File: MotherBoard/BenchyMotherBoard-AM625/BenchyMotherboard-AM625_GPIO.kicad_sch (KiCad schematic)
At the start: 58 parts, among them J14 S3B-XH-A, J17 B10B-XH-A, J2 S4B-XA-SK, U1 AM6254ATCGGAALW, U38 EMC2301-1-ACZL-TR, U58 NCV7357MW3R2G, U65 74LVC541ABQ,115

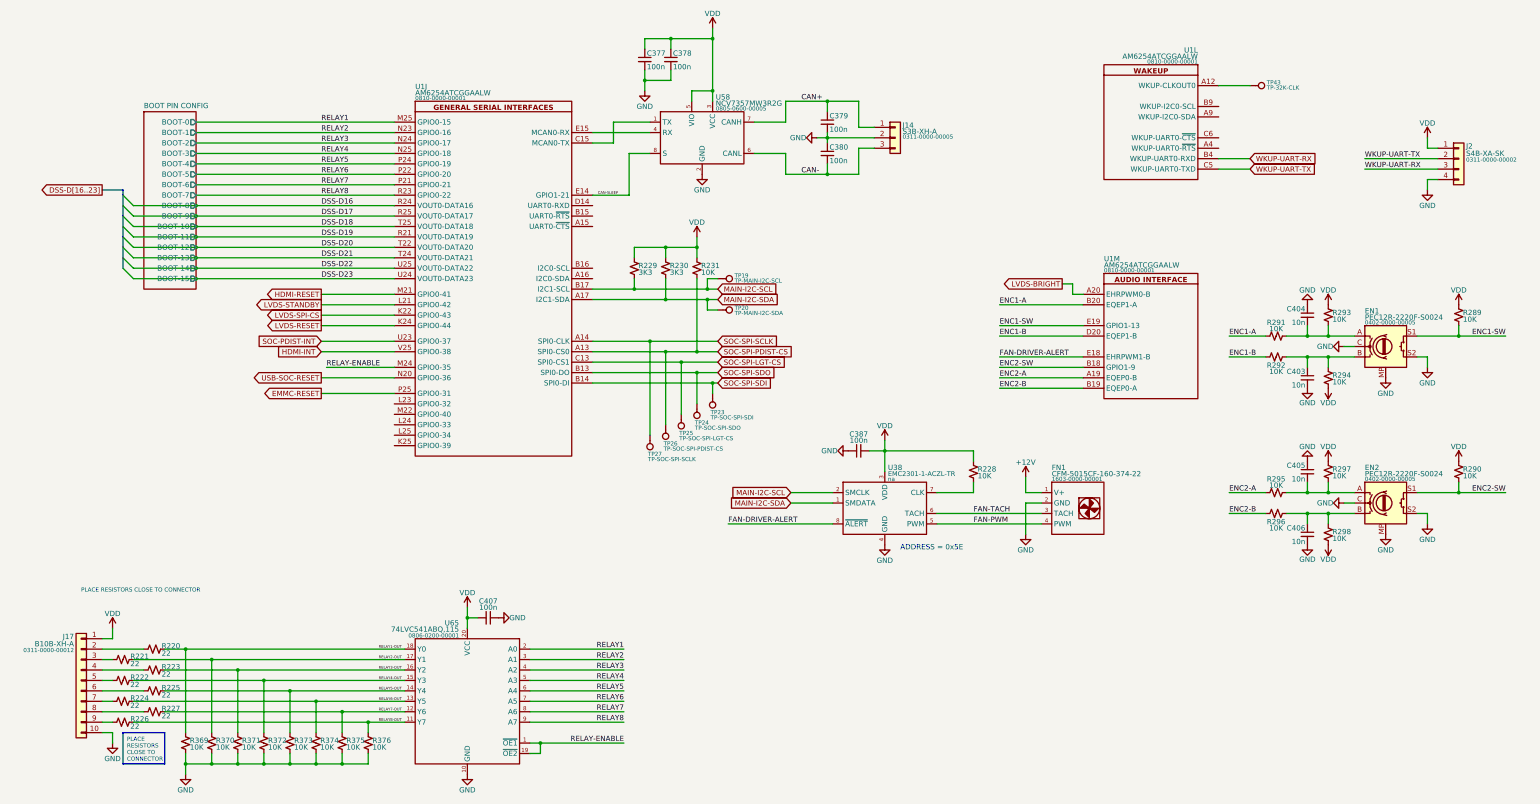
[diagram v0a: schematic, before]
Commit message: Schematic capture mostly complete. Starting PCB layout
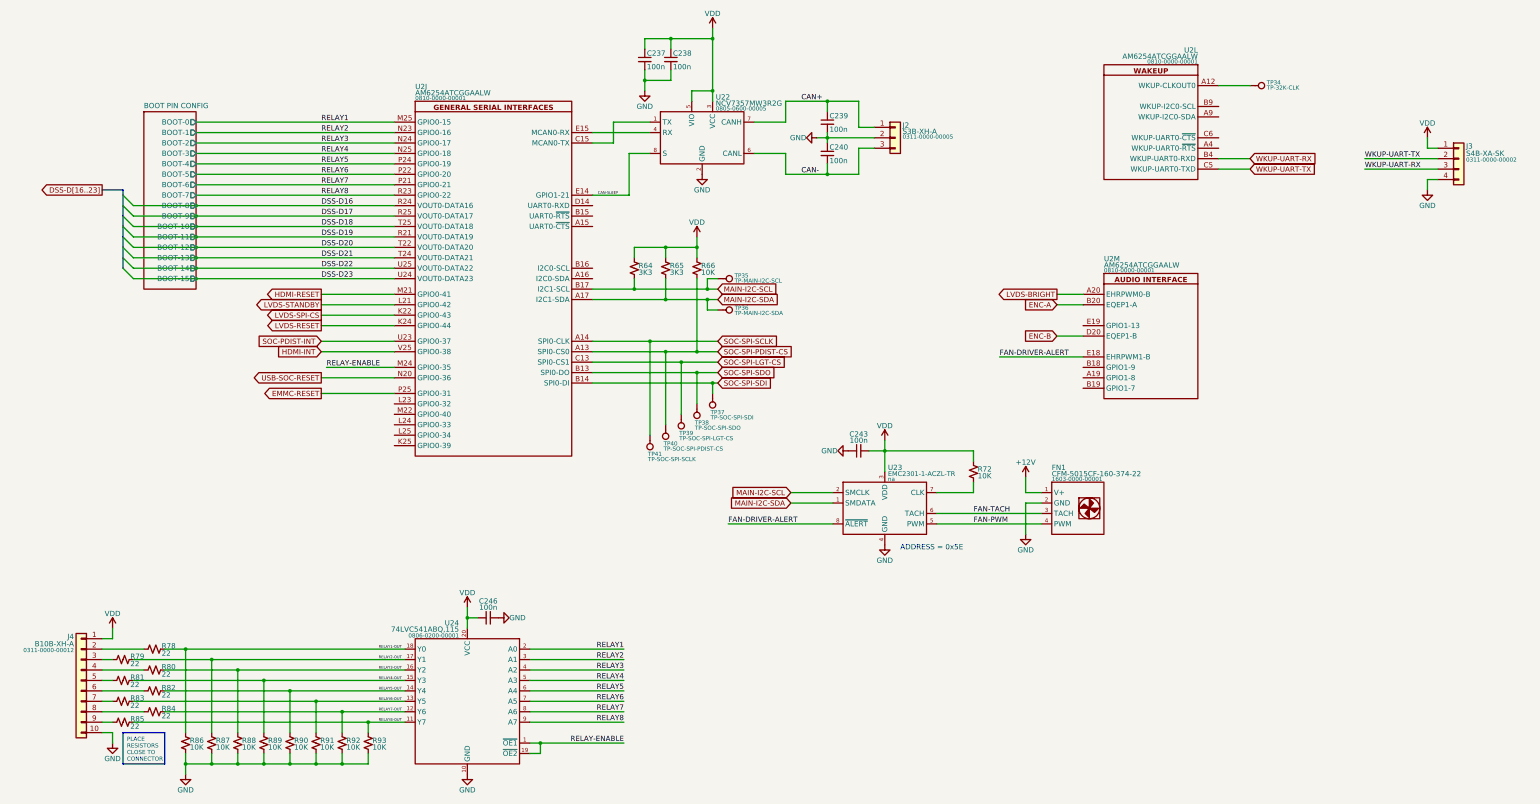
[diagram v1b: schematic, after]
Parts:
- removed C403, C404, C405, C406: 10n, Daxxn_Standard_Capacitors:CAP_0402, symbol DX_Capacitor_Ceramic:CL05B103KB5NNNC
- removed EN1, EN2: PEC12R-2220F-S0024, Daxxn_Controls_Encoders:PEC12R, symbol DX_Control_RotaryEncoder:PEC12R-2220F-S0024
- removed R289, R290, R291, R292, R293, R294, R295, R296, R297, R298: 10K, Daxxn_Standard_Resistors:RES_0402, symbol DX_Resistor:RC0402JR-0710KL
- FN1: footprint Daxxn_Connectors_JST:B4B-XH-A -> Daxxn_Connectors_Header:0470533000
- renumbered C377 to C237, C378 to C238, C379 to C239, C380 to C240, C387 to C243, C407 to C246, J14 to J2, J2 to J3, J17 to J4, R229 to R64, R230 to R65, R231 to R66, R228 to R72, R220 to R78, R221 to R79, R223 to R80, R222 to R81, R225 to R82, R224 to R83, R227 to R84, R226 to R85, R369 to R86, R370 to R87, R371 to R88, R372 to R89, R373 to R90, R374 to R91, R375 to R92, R376 to R93, TP43 to TP34, TP19 to TP35, TP20 to TP36, TP23 to TP37, TP24 to TP38, TP25 to TP39, TP26 to TP40, TP27 to TP41, U1 to U2, U58 to U22, U38 to U23, U65 to U24
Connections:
- net ENC1-A renamed ENC-A
- net ENC1-B renamed ENC-B
- net ENC1-SW: no longer names the net of U2.E19 (MCASP0-AFSR)
- net ENC2-A: no longer names the net of U2.A19 (MCASP0-AXR2)
- net ENC2-B: no longer names the net of U2.B19 (MCASP0-AXR3)
- net ENC2-SW: no longer names the net of U2.B18 (MCASP0-AXR1)
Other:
- note removed: "PLACE RESISTORS CLOSE TO CONNECTOR"
